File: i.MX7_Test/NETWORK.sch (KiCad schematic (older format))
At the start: 2 parts

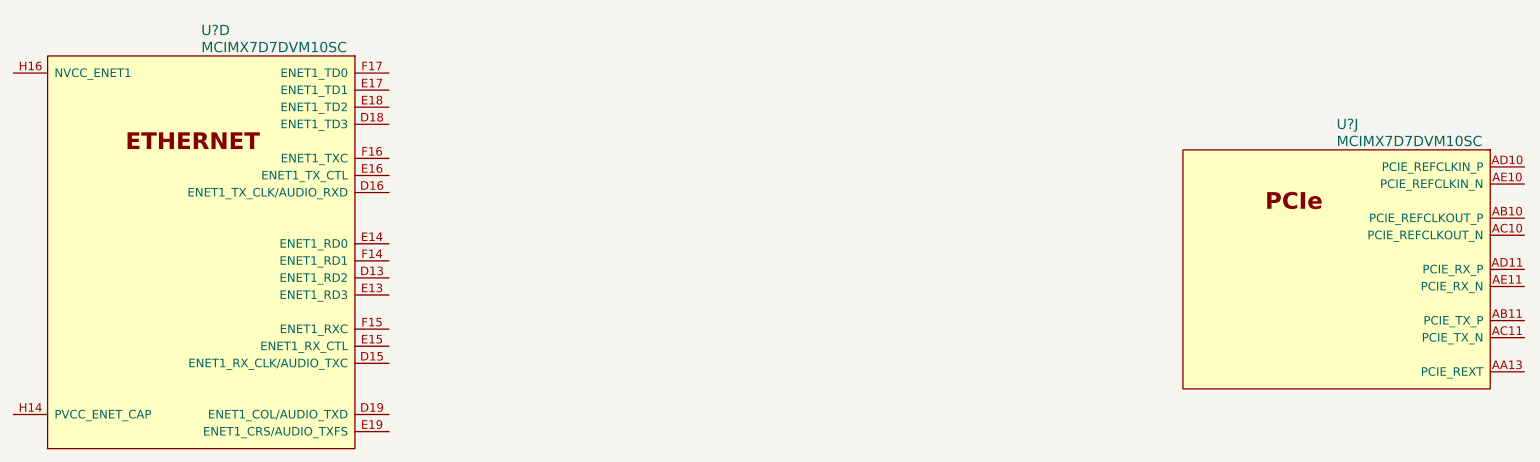
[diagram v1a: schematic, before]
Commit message: Added some schematics for PMIC Added some Documentation for i.mx7
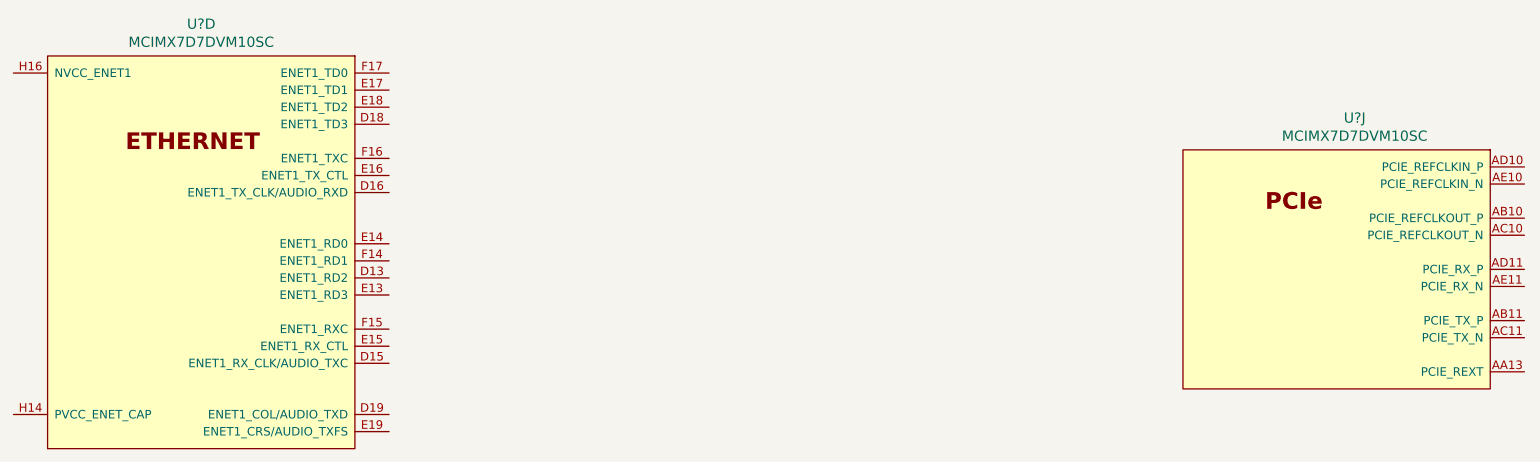
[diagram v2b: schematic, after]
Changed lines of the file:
@@
 LIBS:contrib
 LIBS:valves
-LIBS:ACS
-LIBS:ADV7533
-LIBS:bluetooth
-LIBS:camera1
-LIBS:CC26XX
-LIBS:con-usb
-LIBS:ESP8266 - Kopie
-LIBS:ESP8266
-LIBS:ESS
-LIBS:LMH0030
-LIBS:lora
-LIBS:open-project
-LIBS:s_relays
-LIBS:shield_arduino
-LIBS:silego
-LIBS:siona
-LIBS:STM
-LIBS:stm8
-LIBS:stm32
-LIBS:TFP410
-LIBS:TI
-LIBS:top22xy
-LIBS:TRANSFORMER
-LIBS:USB_c
-LIBS:w_analog
-LIBS:w_connectors
-LIBS:w_device
-LIBS:w_logic
-LIBS:w_memory
-LIBS:w_microcontrollers
-LIBS:w_opto
-LIBS:w_relay
-LIBS:w_rtx
-LIBS:w_transistor
-LIBS:w_vacuum
-LIBS:IMX7D
-LIBS:voltages
-LIBS:pf3000
+LIBS:ip4292cz10-tbr
 LIBS:i.MX7_Test-cache
-EELAYER 25 0
+EELAYER 26 0
 EELAYER END
 $Descr A3 16535 11693
 encoding utf-8
-Sheet 9 10
+Sheet 9 11
 Title ""
 Date ""
@@
 U 4 1 590B374B
 P 4700 3000
-F 0 "U?" H 4700 3000 60  0000 L CNN
-F 1 "MCIMX7D7DVM10SC" H 4700 2900 60  0000 L CNN
+F 0 "U?" H 4700 3037 60  0000 C CNN
+F 1 "MCIMX7D7DVM10SC" H 4700 2931 60  0000 C CNN
 F 2 "" H 2450 4700 60  0001 C CNN
 F 3 "" H 2450 4700 60  0001 C CNN
@@
 U 10 1 590B382E
 P 11350 3550
-F 0 "U?" H 11350 3550 60  0000 L CNN
-F 1 "MCIMX7D7DVM10SC" H 11350 3450 60  0000 L CNN
+F 0 "U?" H 11456 3587 60  0000 C CNN
+F 1 "MCIMX7D7DVM10SC" H 11456 3481 60  0000 C CNN
 F 2 "" H 9100 5250 60  0001 C CNN
 F 3 "" H 9100 5250 60  0001 C CNN
